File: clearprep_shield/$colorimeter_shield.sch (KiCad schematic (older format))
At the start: 7 parts, among them K1 CONN_3, P1 CONN_4, P2 CONN_5X2, P4 CONN_2

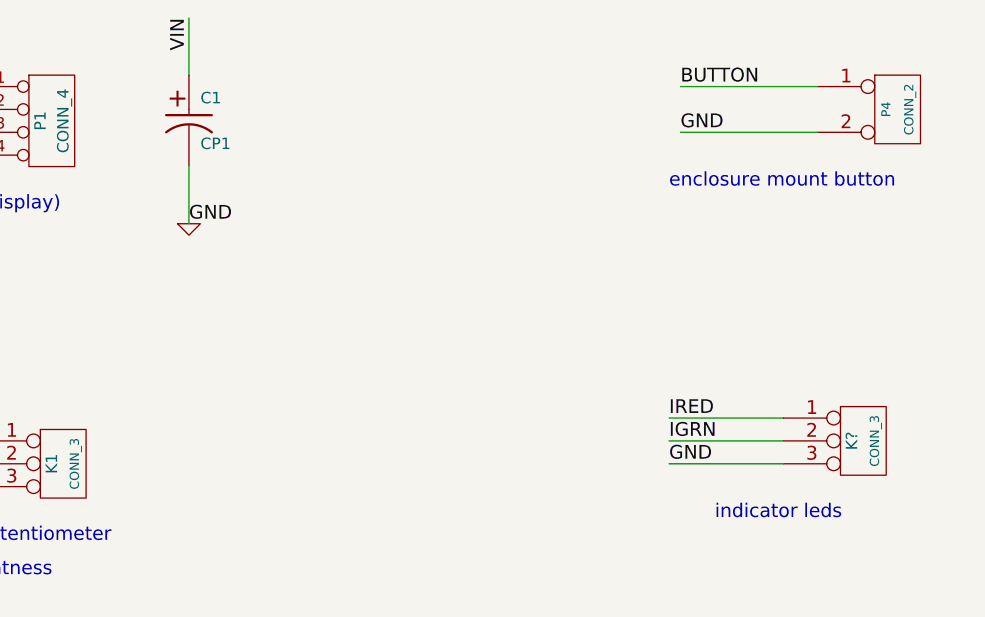
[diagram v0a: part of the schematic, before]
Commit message: Designed ardiuno sheild for clearprep device.
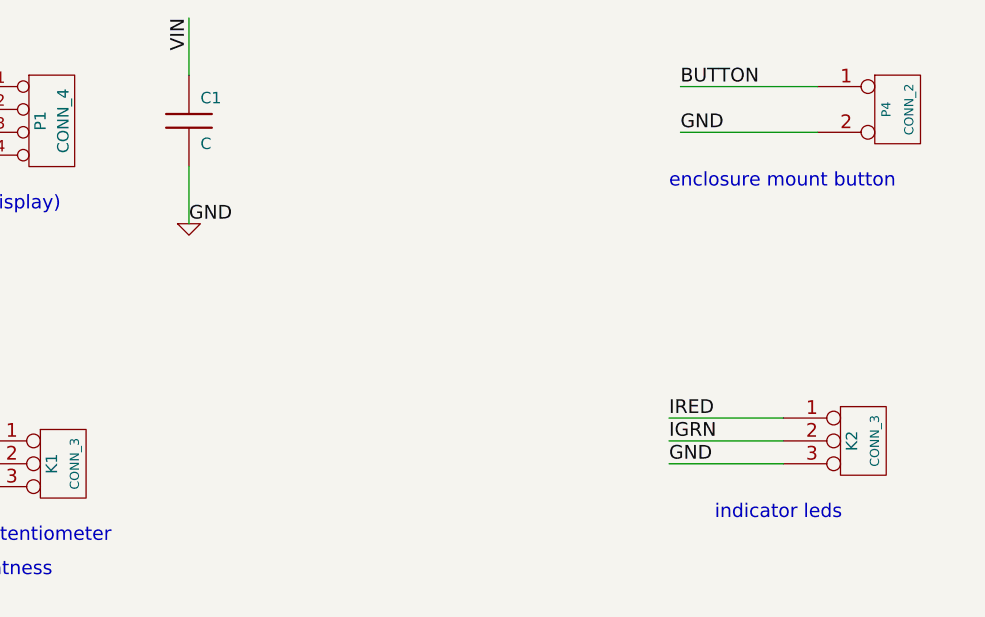
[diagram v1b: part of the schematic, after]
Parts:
- removed C1: CP1, symbol CP1
- added C1: C, symbol C
- gave numbers to parts that had none: 1
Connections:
- net GND: now also C1.2
- net VIN: now also C1.1
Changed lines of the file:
@@
 GND
 $Comp
-L GND #PWR06
+L GND #PWR05
 U 1 1 4F04AA6D
 P 7000 1800
-F 0 "#PWR06" H 7000 1800 30  0001 C CNN
+F 0 "#PWR05" H 7000 1800 30  0001 C CNN
 F 1 "GND" H 7000 1730 30  0001 C CNN
 F 2 "" H 7000 1800 60  0001 C CNN
 F 3 "" H 7000 1800 60  0001 C CNN
 	1    7000 1800
-	1    0    0    -1
-$EndComp
-$Comp
-L CP1 C1
-U 1 1 4F04AA4F
-P 7000 1350
-F 0 "C1" H 7050 1450 50  0000 L CNN
-F 1 "CP1" H 7050 1250 50  0000 L CNN
-F 2 "" H 7000 1350 60  0001 C CNN
-F 3 "" H 7000 1350 60  0001 C CNN
-	1    7000 1350
 	1    0    0    -1
 $EndComp
@@
 IGRN
 $Comp
-L CONN_3 K?
+L CONN_3 K2
 U 1 1 51B8E61C
 P 9950 2750
-F 0 "K?" V 9900 2750 50  0000 C CNN
+F 0 "K2" V 9900 2750 50  0000 C CNN
 F 1 "CONN_3" V 10000 2750 40  0000 C CNN
 F 2 "" H 9950 2750 60  0000 C CNN
@@
 Text Label 9100 2650 0    60   ~ 0
 IRED
+$Comp
+L C C1
+U 1 1 51B8E8C5
+P 7000 1350
+F 0 "C1" H 7050 1450 50  0000 L CNN
+F 1 "C" H 7050 1250 50  0000 L CNN
+F 2 "" H 7000 1350 60  0000 C CNN
+F 3 "" H 7000 1350 60  0000 C CNN
+	1    7000 1350
+	1    0    0    -1
+$EndComp
 $EndSCHEMATC
